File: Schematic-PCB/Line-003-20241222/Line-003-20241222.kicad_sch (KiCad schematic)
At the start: 223 parts, among them J1 VIN, J2 Conn_MD, SW1 RESET, U47 LM393, U48 LM393, U49 LM393, U50 LM393, U51 LM393, U52 LM393, U53 LM393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

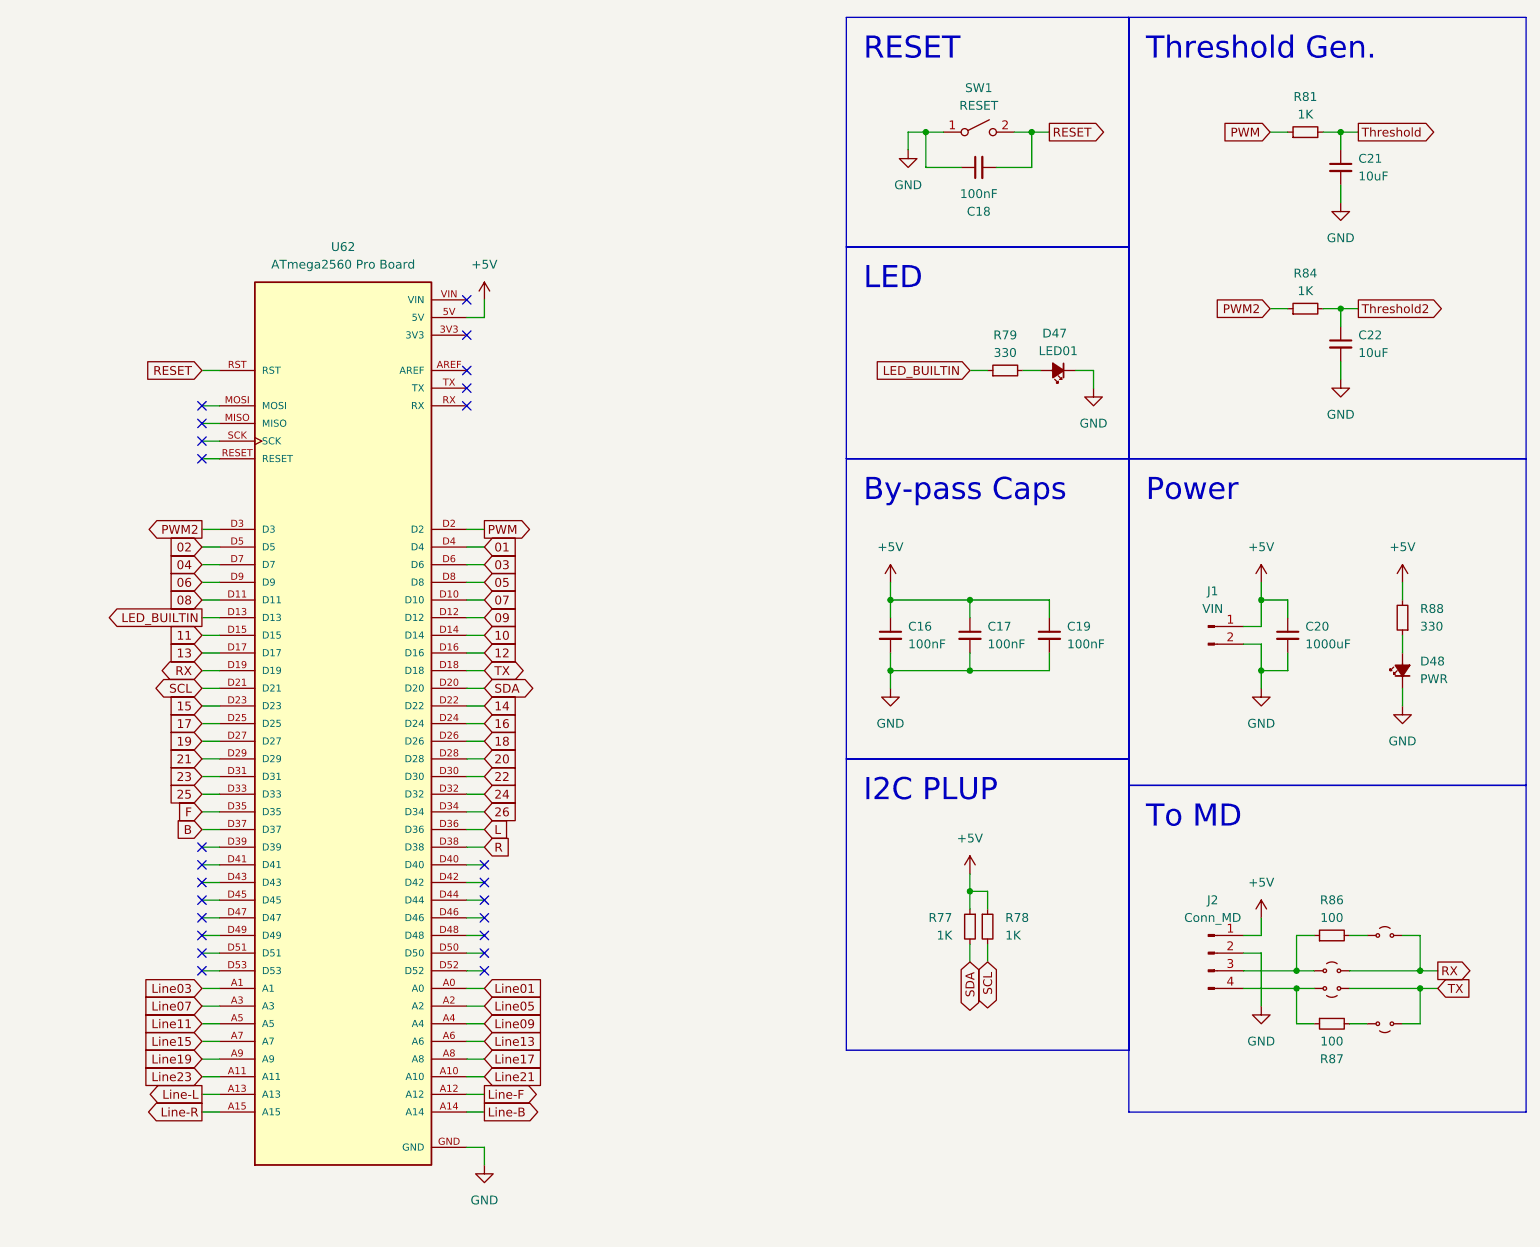
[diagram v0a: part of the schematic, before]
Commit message: update: ラインセンサ基板のPCBを更新した
配線を進めた
Thをベタ化して配線を楽にした
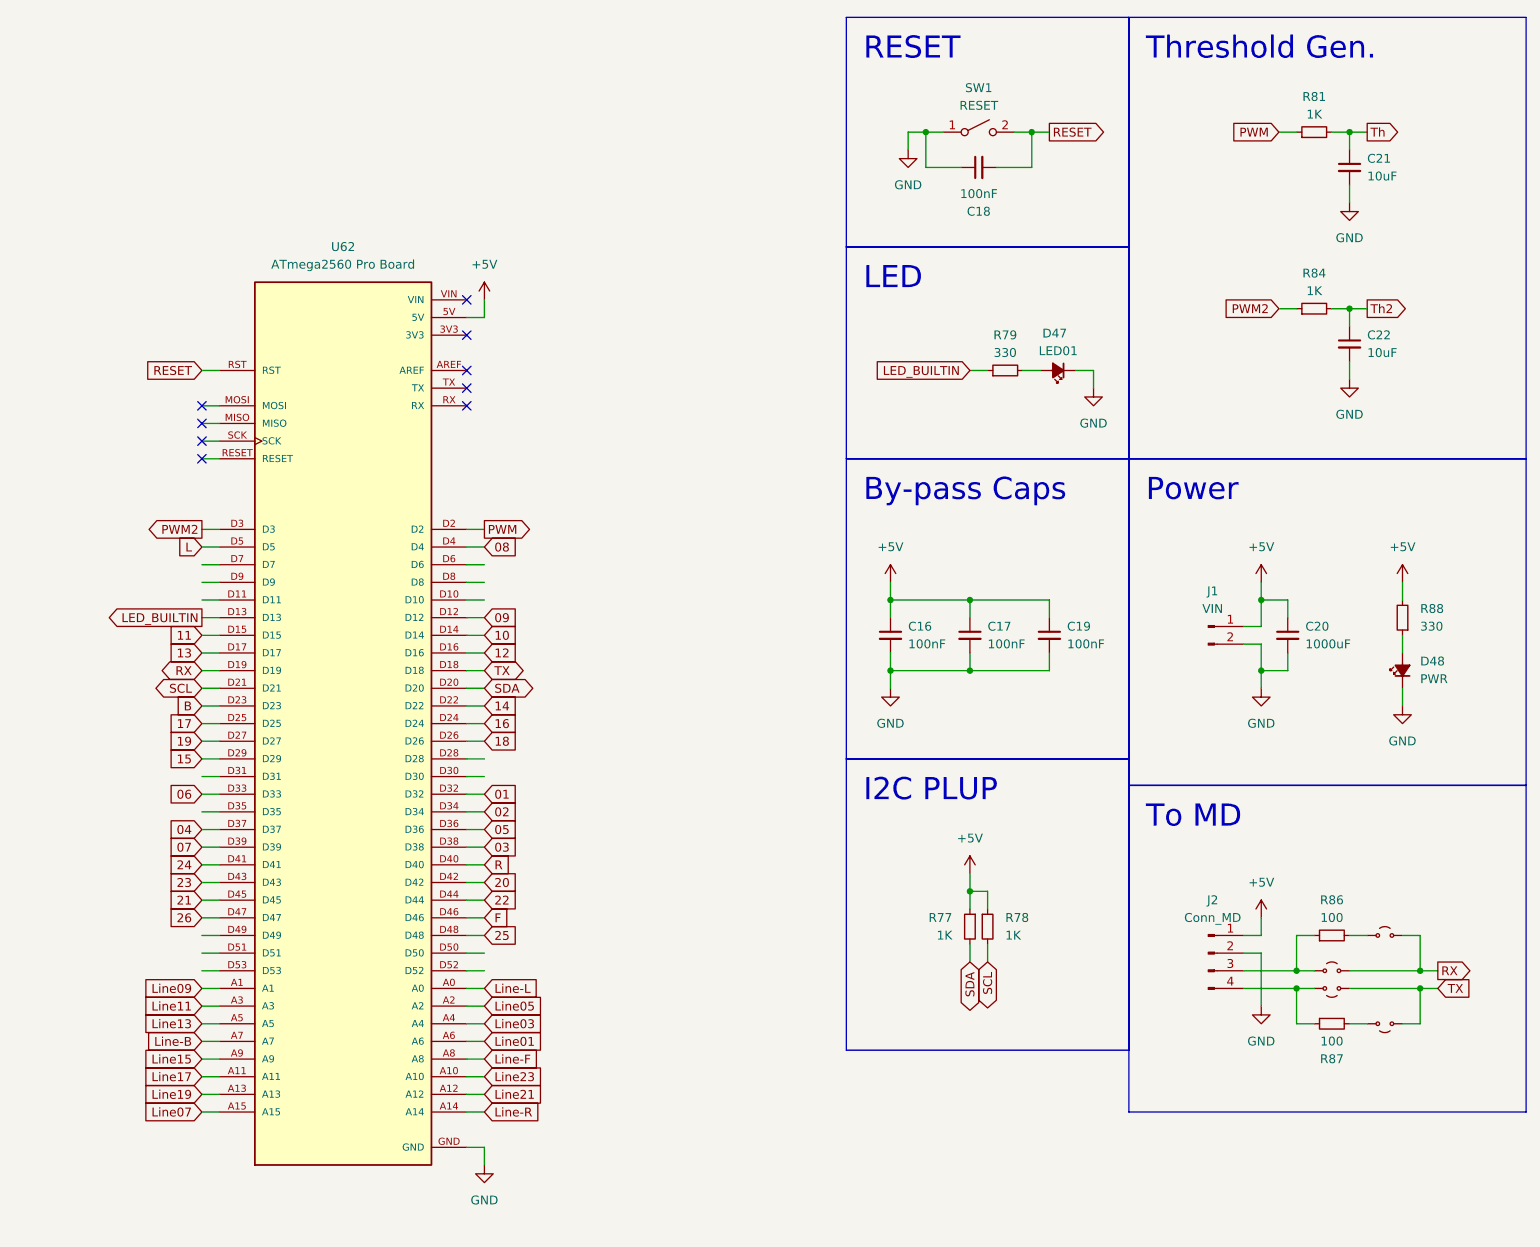
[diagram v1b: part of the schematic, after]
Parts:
- J1: footprint Connector_JST:JST_XH_B2B-XH-A_1x02_P2.50mm_Vertical -> Connector_JST:JST_XH_S2B-XH-A-1_1x02_P2.50mm_Horizontal
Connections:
- net Threshold is gone; now on net Th: C21.1, R81.2
- net Threshold2 is gone; now on net Th2: C22.1, R84.2
- net 01: now also U62.D32; no longer U62.D4
- net 02: now also U62.D34; no longer U62.D5
- net 03: now also U62.D38; no longer U62.D6
- net 04: now also U62.D37; no longer U62.D7
- net 05: now also U62.D36; no longer U62.D8
- net 06: now also U62.D33; no longer U62.D9
- net 07: now also U62.D39; no longer U62.D10
- net 08: now also U62.D4; no longer U62.D11
- net 15: now also U62.D29; no longer U62.D23
- net 20: now also U62.D42; no longer U62.D28
- net 21: now also U62.D45; no longer U62.D29
- net 22: now also U62.D44; no longer U62.D30
- net 23: now also U62.D43; no longer U62.D31
- net 24: now also U62.D41; no longer U62.D32
- net 25: now also U62.D48; no longer U62.D33
- net 26: now also U62.D47; no longer U62.D34
- net B: now also U62.D23; no longer U62.D37
- net F: now also U62.D46; no longer U62.D35
- net L: now also U62.D5; no longer U62.D36
- net Line-B: now also U62.A7; no longer U62.A14
- net Line-F: now also U62.A8; no longer U62.A12
- net Line-L: now also U62.A0; no longer U62.A13
- net Line-R: now also U62.A14; no longer U62.A15
- net Line01: now also U62.A6; no longer U62.A0
- net Line03: now also U62.A4; no longer U62.A1
- net Line07: now also U62.A15; no longer U62.A3
- net Line09: now also U62.A1; no longer U62.A4
- net Line11: now also U62.A3; no longer U62.A5
- net Line13: now also U62.A5; no longer U62.A6
- net Line15: now also U62.A9; no longer U62.A7
- net Line17: now also U62.A11; no longer U62.A8
- net Line19: now also U62.A13; no longer U62.A9
- net Line21: now also U62.A12; no longer U62.A10
- net Line23: now also U62.A10; no longer U62.A11
- net R: now also U62.D40; no longer U62.D38
- no-connect marks 24 -> 9
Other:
- moved on the sheet: C21, C22, R81, R84

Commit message: update: ラインセンサ基板の1次DRを完了させ、発注用ファイルを出力した
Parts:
- SW1: footprint (none) -> @2024TOINIOT2-Line:Tactile1
- U47, U48, U49, U50, U51, U52, U53, U54, U55, U56, U57, U58, U59, U60, U61: footprint Package_SO:SOIC-8_3.9x4.9mm_P1.27mm -> Package_SO:SOP-8_3.9x4.9mm_P1.27mm
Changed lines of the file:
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@@
 			)
 		)
-		(property "Footprint" "Package_SO:SOIC-8_3.9x4.9mm_P1.27mm"
+		(property "Footprint" "Package_SO:SOP-8_3.9x4.9mm_P1.27mm"
 			(at 203.2 80.01 0)
 			(effects
@@
 			)
 		)
-		(property "Footprint" "Package_SO:SOIC-8_3.9x4.9mm_P1.27mm"
+		(property "Footprint" "Package_SO:SOP-8_3.9x4.9mm_P1.27mm"
 			(at 203.2 213.36 0)
 			(effects
@@
 			)
 		)
-		(property "Footprint" "Package_SO:SOIC-8_3.9x4.9mm_P1.27mm"
+		(property "Footprint" "Package_SO:SOP-8_3.9x4.9mm_P1.27mm"
 			(at 259.08 321.31 0)
 			(effects
@@
 			)
 		)
-		(property "Footprint" "Package_SO:SOIC-8_3.9x4.9mm_P1.27mm"
+		(property "Footprint" "Package_SO:SOP-8_3.9x4.9mm_P1.27mm"
 			(at 203.2 124.46 0)
 			(effects
@@
 			)
 		)
-		(property "Footprint" "Package_SO:SOIC-8_3.9x4.9mm_P1.27mm"
+		(property "Footprint" "Package_SO:SOP-8_3.9x4.9mm_P1.27mm"
 			(at 259.08 35.56 0)
 			(effects
@@
 			)
 		)
-		(property "Footprint" "Package_SO:SOIC-8_3.9x4.9mm_P1.27mm"
+		(property "Footprint" "Package_SO:SOP-8_3.9x4.9mm_P1.27mm"
 			(at 203.2 35.56 0)
 			(effects
@@
 			)
 		)
-		(property "Footprint" "Package_SO:SOIC-8_3.9x4.9mm_P1.27mm"
+		(property "Footprint" "Package_SO:SOP-8_3.9x4.9mm_P1.27mm"
 			(at 227.33 266.7 0)
 			(effects
@@
 			)
 		)
-		(property "Footprint" "Package_SO:SOIC-8_3.9x4.9mm_P1.27mm"
+		(property "Footprint" "Package_SO:SOP-8_3.9x4.9mm_P1.27mm"
 			(at 203.2 187.96 0)
 			(effects
@@
 			)
 		)
-		(property "Footprint" "Package_SO:SOIC-8_3.9x4.9mm_P1.27mm"
+		(property "Footprint" "Package_SO:SOP-8_3.9x4.9mm_P1.27mm"
 			(at 227.33 177.8 0)
 			(effects
@@
 			)
 		)
-		(property "Footprint" "Package_SO:SOIC-8_3.9x4.9mm_P1.27mm"
+		(property "Footprint" "Package_SO:SOP-8_3.9x4.9mm_P1.27mm"
 			(at 227.33 222.25 0)
 			(effects
@@
 			)
 		)
-		(property "Footprint" "Package_SO:SOIC-8_3.9x4.9mm_P1.27mm"
+		(property "Footprint" "Package_SO:SOP-8_3.9x4.9mm_P1.27mm"
 			(at 203.2 257.81 0)
 			(effects
@@
 			)
 		)
-		(property "Footprint" "Package_SO:SOIC-8_3.9x4.9mm_P1.27mm"
+		(property "Footprint" "Package_SO:SOP-8_3.9x4.9mm_P1.27mm"
 			(at 283.21 44.45 0)
 			(effects
@@
 			)
 		)
-		(property "Footprint" "Package_SO:SOIC-8_3.9x4.9mm_P1.27mm"
+		(property "Footprint" "Package_SO:SOP-8_3.9x4.9mm_P1.27mm"
 			(at 259.08 302.26 0)
 			(effects
@@
 			)
 		)
-		(property "Footprint" ""
+		(property "Footprint" "@2024TOINIOT2-Line:Tactile1"
 			(at 502.92 29.21 0)
 			(effects
@@
 			)
 		)
-		(property "Footprint" "Package_SO:SOIC-8_3.9x4.9mm_P1.27mm"
+		(property "Footprint" "Package_SO:SOP-8_3.9x4.9mm_P1.27mm"
 			(at 203.2 276.86 0)
 			(effects
@@
 			)
 		)
-		(property "Footprint" "Package_SO:SOIC-8_3.9x4.9mm_P1.27mm"
+		(property "Footprint" "Package_SO:SOP-8_3.9x4.9mm_P1.27mm"
 			(at 203.2 54.61 0)
 			(effects
@@
 			)
 		)
-		(property "Footprint" "Package_SO:SOIC-8_3.9x4.9mm_P1.27mm"
+		(property "Footprint" "Package_SO:SOP-8_3.9x4.9mm_P1.27mm"
 			(at 283.21 222.25 0)
 			(effects
@@
 			)
 		)
-		(property "Footprint" "Package_SO:SOIC-8_3.9x4.9mm_P1.27mm"
+		(property "Footprint" "Package_SO:SOP-8_3.9x4.9mm_P1.27mm"
 			(at 203.2 346.71 0)
 			(effects
@@
 			)
 		)
-		(property "Footprint" "Package_SO:SOIC-8_3.9x4.9mm_P1.27mm"
+		(property "Footprint" "Package_SO:SOP-8_3.9x4.9mm_P1.27mm"
 			(at 203.2 232.41 0)
 			(effects
@@
 			)
 		)
-		(property "Footprint" "Package_SO:SOIC-8_3.9x4.9mm_P1.27mm"
+		(property "Footprint" "Package_SO:SOP-8_3.9x4.9mm_P1.27mm"
 			(at 259.08 232.41 0)
 			(effects
@@
 			)
 		)
-		(property "Footprint" "Package_SO:SOIC-8_3.9x4.9mm_P1.27mm"
+		(property "Footprint" "Package_SO:SOP-8_3.9x4.9mm_P1.27mm"
 			(at 259.08 257.81 0)
 			(effects
@@
 			)
 		)
-		(property "Footprint" "Package_SO:SOIC-8_3.9x4.9mm_P1.27mm"
+		(property "Footprint" "Package_SO:SOP-8_3.9x4.9mm_P1.27mm"
 			(at 259.08 124.46 0)
 			(effects
@@
 			)
 		)
-		(property "Footprint" "Package_SO:SOIC-8_3.9x4.9mm_P1.27mm"
+		(property "Footprint" "Package_SO:SOP-8_3.9x4.9mm_P1.27mm"
 			(at 259.08 187.96 0)
 			(effects
@@
 			)
 		)
-		(property "Footprint" "Package_SO:SOIC-8_3.9x4.9mm_P1.27mm"
+		(property "Footprint" "Package_SO:SOP-8_3.9x4.9mm_P1.27mm"
 			(at 203.2 321.31 0)
 			(effects
@@
 			)
 		)
-		(property "Footprint" "Package_SO:SOIC-8_3.9x4.9mm_P1.27mm"
+		(property "Footprint" "Package_SO:SOP-8_3.9x4.9mm_P1.27mm"
 			(at 227.33 88.9 0)
 			(effects
@@
 			)
 		)
-		(property "Footprint" "Package_SO:SOIC-8_3.9x4.9mm_P1.27mm"
+		(property "Footprint" "Package_SO:SOP-8_3.9x4.9mm_P1.27mm"
 			(at 283.21 88.9 0)
 			(effects
@@
 			)
 		)
-		(property "Footprint" "Package_SO:SOIC-8_3.9x4.9mm_P1.27mm"
+		(property "Footprint" "Package_SO:SOP-8_3.9x4.9mm_P1.27mm"
 			(at 259.08 168.91 0)
 			(effects
@@
 			)
 		)
-		(property "Footprint" "Package_SO:SOIC-8_3.9x4.9mm_P1.27mm"
+		(property "Footprint" "Package_SO:SOP-8_3.9x4.9mm_P1.27mm"
 			(at 259.08 276.86 0)
 			(effects
@@
 			)
 		)
-		(property "Footprint" "Package_SO:SOIC-8_3.9x4.9mm_P1.27mm"
+		(property "Footprint" "Package_SO:SOP-8_3.9x4.9mm_P1.27mm"
 			(at 259.08 80.01 0)
 			(effects
@@
 			)
 		)
-		(property "Footprint" "Package_SO:SOIC-8_3.9x4.9mm_P1.27mm"
+		(property "Footprint" "Package_SO:SOP-8_3.9x4.9mm_P1.27mm"
 			(at 203.2 143.51 0)
 			(effects
@@
 			)
 		)
-		(property "Footprint" "Package_SO:SOIC-8_3.9x4.9mm_P1.27mm"
+		(property "Footprint" "Package_SO:SOP-8_3.9x4.9mm_P1.27mm"
 			(at 283.21 133.35 0)
 			(effects
@@
 			)
 		)
-		(property "Footprint" "Package_SO:SOIC-8_3.9x4.9mm_P1.27mm"
+		(property "Footprint" "Package_SO:SOP-8_3.9x4.9mm_P1.27mm"
 			(at 259.08 143.51 0)
 			(effects
@@
 			)
 		)
-		(property "Footprint" "Package_SO:SOIC-8_3.9x4.9mm_P1.27mm"
+		(property "Footprint" "Package_SO:SOP-8_3.9x4.9mm_P1.27mm"
 			(at 227.33 44.45 0)
 			(effects
@@
 			)
 		)
-		(property "Footprint" "Package_SO:SOIC-8_3.9x4.9mm_P1.27mm"
+		(property "Footprint" "Package_SO:SOP-8_3.9x4.9mm_P1.27mm"
 			(at 203.2 99.06 0)
 			(effects
@@
 			)
 		)
-		(property "Footprint" "Package_SO:SOIC-8_3.9x4.9mm_P1.27mm"
+		(property "Footprint" "Package_SO:SOP-8_3.9x4.9mm_P1.27mm"
 			(at 259.08 213.36 0)
 			(effects
@@
 			)
 		)
-		(property "Footprint" "Package_SO:SOIC-8_3.9x4.9mm_P1.27mm"
+		(property "Footprint" "Package_SO:SOP-8_3.9x4.9mm_P1.27mm"
 			(at 259.08 54.61 0)
 			(effects
@@
 			)
 		)
-		(property "Footprint" "Package_SO:SOIC-8_3.9x4.9mm_P1.27mm"
+		(property "Footprint" "Package_SO:SOP-8_3.9x4.9mm_P1.27mm"
 			(at 283.21 177.8 0)
 			(effects
@@
 			)
 		)
-		(property "Footprint" "Package_SO:SOIC-8_3.9x4.9mm_P1.27mm"
+		(property "Footprint" "Package_SO:SOP-8_3.9x4.9mm_P1.27mm"
 			(at 203.2 365.76 0)
 			(effects
@@
 			)
 		)
-		(property "Footprint" "Package_SO:SOIC-8_3.9x4.9mm_P1.27mm"
+		(property "Footprint" "Package_SO:SOP-8_3.9x4.9mm_P1.27mm"
 			(at 203.2 302.26 0)
 			(effects
@@
 			)
 		)
-		(property "Footprint" "Package_SO:SOIC-8_3.9x4.9mm_P1.27mm"
+		(property "Footprint" "Package_SO:SOP-8_3.9x4.9mm_P1.27mm"
 			(at 227.33 311.15 0)
 			(effects
@@
 			)
 		)
-		(property "Footprint" "Package_SO:SOIC-8_3.9x4.9mm_P1.27mm"
+		(property "Footprint" "Package_SO:SOP-8_3.9x4.9mm_P1.27mm"
 			(at 203.2 168.91 0)
 			(effects
@@
 			)
 		)
-		(property "Footprint" "Package_SO:SOIC-8_3.9x4.9mm_P1.27mm"
+		(property "Footprint" "Package_SO:SOP-8_3.9x4.9mm_P1.27mm"
 			(at 283.21 266.7 0)
 			(effects
@@
 			)
 		)
-		(property "Footprint" "Package_SO:SOIC-8_3.9x4.9mm_P1.27mm"
+		(property "Footprint" "Package_SO:SOP-8_3.9x4.9mm_P1.27mm"
 			(at 227.33 355.6 0)
 			(effects
@@
 			)
 		)
-		(property "Footprint" "Package_SO:SOIC-8_3.9x4.9mm_P1.27mm"
+		(property "Footprint" "Package_SO:SOP-8_3.9x4.9mm_P1.27mm"
 			(at 227.33 133.35 0)
 			(effects
@@
 			)
 		)
-		(property "Footprint" "Package_SO:SOIC-8_3.9x4.9mm_P1.27mm"
+		(property "Footprint" "Package_SO:SOP-8_3.9x4.9mm_P1.27mm"
 			(at 259.08 99.06 0)
 			(effects
@@
 			)
 		)
-		(property "Footprint" "Package_SO:SOIC-8_3.9x4.9mm_P1.27mm"
+		(property "Footprint" "Package_SO:SOP-8_3.9x4.9mm_P1.27mm"
 			(at 283.21 311.15 0)
 			(effects
